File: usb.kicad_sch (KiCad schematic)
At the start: 55 parts, among them J901 AU-Y1008-2-BLK, J902 AU-Y1008-2-BLK, U901 USB2514B/M2, U902 AP22966DC8-7, U903 AP22966DC8-7, U904 USBLC6-2SC6, U905 USBLC6-2SC6, U906 USBLC6-2SC6, U907 USBLC6-2SC6, Y901 24 MHz

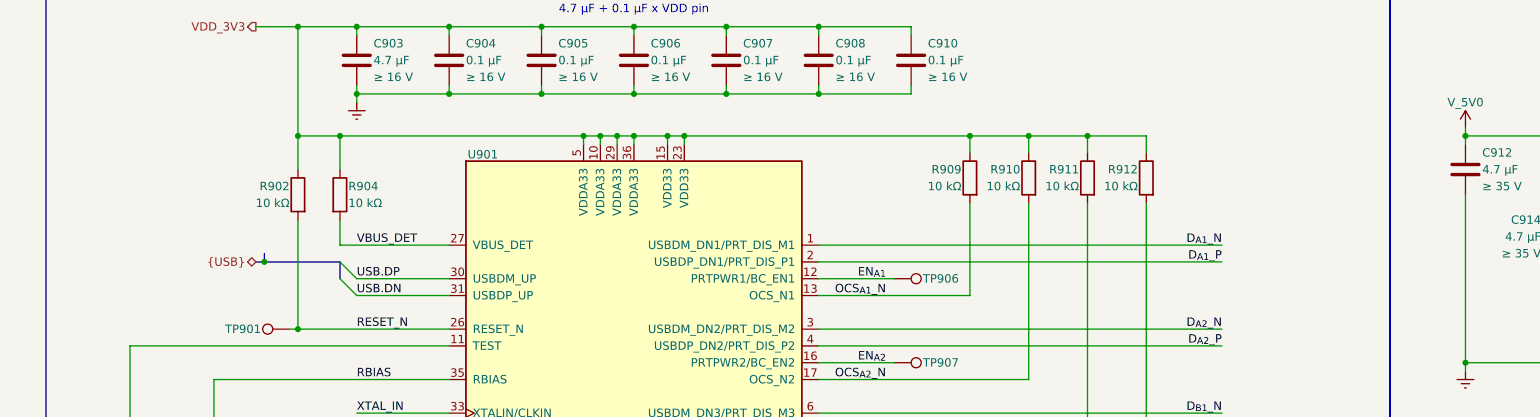
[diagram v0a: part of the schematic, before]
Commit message: Redo MPU pinout using STM32CubeMx
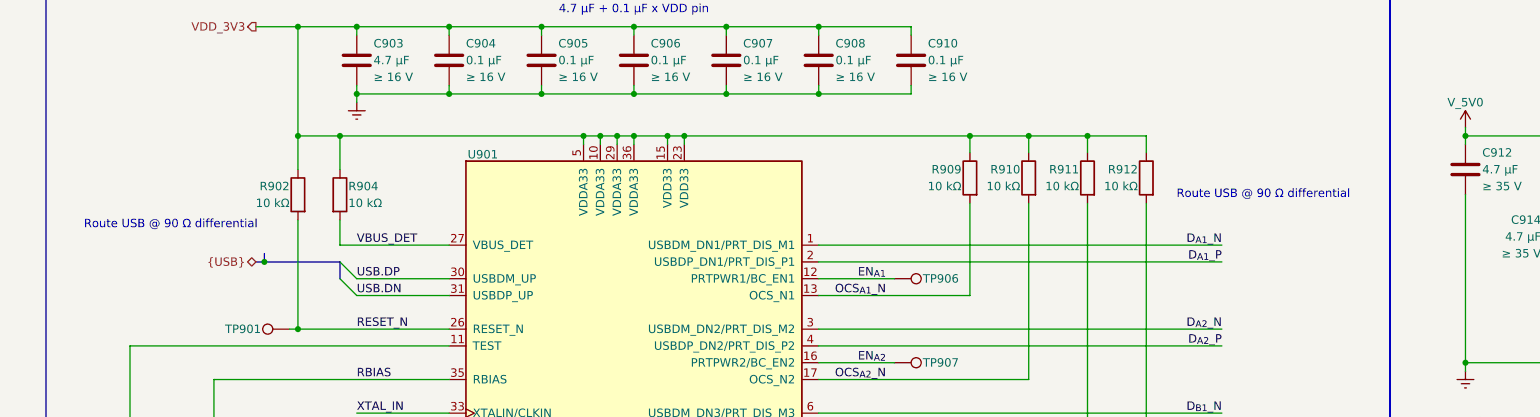
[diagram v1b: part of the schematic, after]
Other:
- note added: "Route USB @ 90 Ω differential"
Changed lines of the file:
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@@
 		)
 	)
+	(text "Route USB @ 90 Ω differential"
+		(exclude_from_sim no)
+		(at 183.642 114.3 0)
+		(effects
+			(font
+				(size 1.27 1.27)
+				(color 194 0 194 1)
+			)
+			(justify left)
+		)
+	)
 	(text "4.7 µF + 0.1 µF x VDD pin"
 		(exclude_from_sim no)
@@
 		)
 	)
+	(text "Route USB @ 90 Ω differential"
+		(exclude_from_sim no)
+		(at 44.704 118.872 0)
+		(effects
+			(font
+				(size 1.27 1.27)
+				(color 194 0 194 1)
+			)
+			(justify right)
+		)
+	)
 	(text "Ports A[0..1]"
 		(exclude_from_sim no)
@@
 		)
 		(property "Netclass" "USB"
-			(at 46.4185 120.65 0)
+			(at 45.0215 120.65 0)
 			(effects
 				(font
 					(size 1.27 1.27)
 				)
-				(justify left)
+				(justify right)
 			)
 		)
 		(property "Component Class" ""
-			(at 137.16 12.7 0)
+			(at -45.72 12.7 0)
 			(effects
 				(font
@@
 					(italic yes)
 				)
-				(justify left)
+				(justify right)
 			)
 		)

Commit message: Add additional info to passives
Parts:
- removed C920, C921, C922, C923: 220 µF, symbol Device:C
- added C920, C921, C922, C923: 220 µF, symbol Device:C_Polarized
- C901, C902, C904, C905, C906, C907, C908, C910: Size (none) -> 0402; Temperature coefficient (none) -> X5R; Tolerance (none) -> 20 %; Voltage rating ≥ 16 V -> 16 V
- C903: Size (none) -> 0603; Temperature coefficient (none) -> X5R; Tolerance (none) -> 20 %; Voltage rating ≥ 16 V -> 35 V
- C909, C911: Size (none) -> 0402; Tolerance (none) -> 2 %; Voltage rating (none) -> 35 V
- C912, C913, C914, C915: Size (none) -> 0603; Temperature coefficient (none) -> X5R; Tolerance (none) -> 20 %; Voltage rating ≥ 35 V -> 35 V
- C916, C917, C918, C919: Size (none) -> 0402; Temperature coefficient (none) -> X5R; Tolerance (none) -> 20 %; Voltage rating ≥ 35 V -> 35 V
- R901: Power rating (none) -> 0.1 W; Size (none) -> 0402; Tolerance ± 1 % -> 1 %
- R902, R904, R908, R909, R910, R911, R912: MPN 560112110020 -> (none); Manufacturer Würth Elektronik -> (none); Power rating (none) -> 0.1 W; Size (none) -> 0402; Tolerance (none) -> 1 %
- R903, R905, R906, R907: MPN 560112110019 -> (none); Manufacturer Würth Elektronik -> (none); Power rating (none) -> 0.1 W; Size (none) -> 0402; Tolerance (none) -> 1 %
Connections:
- net GND: now also C920.2, C921.2, C922.2, C923.2
- net NON_REM0: now also R908.1; no longer R908.2
- net V_BUS_{A1}: now also C920.1
- net V_BUS_{A2}: now also C922.1
- net V_BUS_{B1}: now also C921.1
- net V_BUS_{B2}: now also C923.1
- net at D901.2 (A): now also R908.2; no longer R908.1

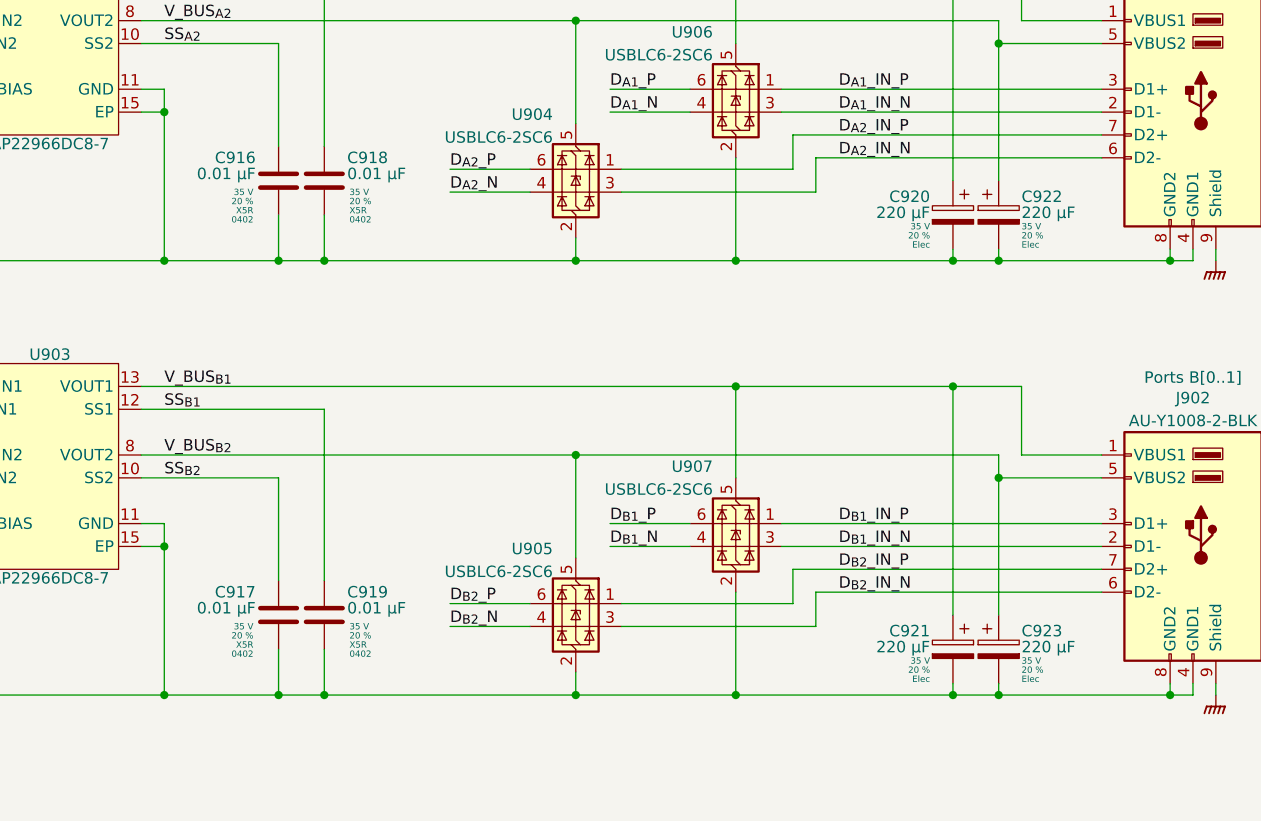
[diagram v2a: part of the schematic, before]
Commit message: Update capacitor BOM
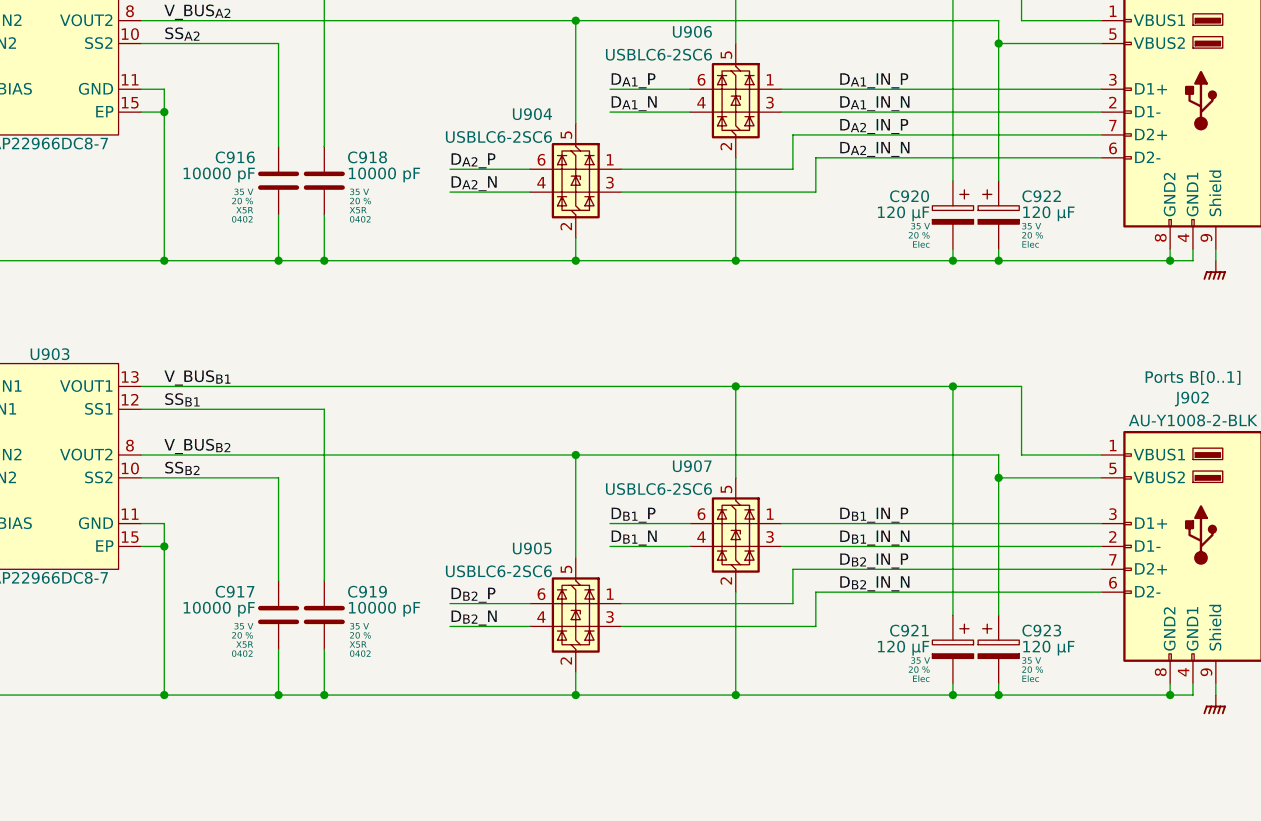
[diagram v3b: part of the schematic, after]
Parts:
- C901, C902, C904, C905, C906, C907, C908, C910: footprint (none) -> perfect_footprints:C_0402_1005Metric; Digi-Key Part Number (none) -> 490-10700-1-ND; MPN (none) -> GRM155R71H104KE14D; Manufacturer (none) -> Murata Electronics
- C903, C912, C913, C914, C915: footprint (none) -> Capacitor_SMD:C_0603_1608Metric; Digi-Key Part Number (none) -> 490-7205-1-ND; MPN (none) -> GRM188R6YA475KE15D; Manufacturer (none) -> Murata Electronics
- C909, C911: footprint (none) -> perfect_footprints:C_0402_1005Metric; Digi-Key Part Number (none) -> 490-3109-1-ND; MPN (none) -> GJM1555C1H8R0CB01D; Manufacturer (none) -> Murata Electronics
- C916, C917, C918, C919: value 0.01 µF -> 10000 pF; footprint (none) -> perfect_footprints:C_0402_1005Metric; Digi-Key Part Number (none) -> 490-4516-1-ND; MPN (none) -> GRM155R71H103KA88D; Manufacturer (none) -> Murata Electronics
- C920, C921, C922, C923: value 220 µF -> 120 µF; footprint (none) -> Capacitor_THT:C_Radial_D8.0mm_H11.5mm_P3.50mm; Digi-Key Part Number (none) -> 732-8943-1-ND; MPN (none) -> 860020574009; Manufacturer (none) -> Würth Elektronik

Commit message: Update R & L BOM
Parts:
- R901: Digi-Key Part Number (none) -> P12.1KLCT-ND; MPN (none) -> ERJ-2RKF1212X; Manufacturer (none) -> Panasonic Electronic Components
- R902, R904, R909, R910, R911, R912: Digi-Key Part Number (none) -> P10.0KLCT-ND; MPN (none) -> ERJ-2RKF1002X; Manufacturer (none) -> Panasonic Electronic Components
- R903, R905, R906, R907: Digi-Key Part Number (none) -> P100KLCT-ND; MPN (none) -> ERJ-2RKF1003X; Manufacturer (none) -> Panasonic Electronic Components
- R908: Digi-Key Part Number (none) -> P1.00KLCT-ND; MPN (none) -> ERJ-2RKF1001X; Manufacturer (none) -> Panasonic Electronic Components

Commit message: Fill BOM info
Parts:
- D901: Digi-Key Part Number (none) -> 732-4978-1-ND
- Y901: footprint (none) -> Crystal:Crystal_SMD_3225-4Pin_3.2x2.5mm; Digi-Key Part Number (none) -> 50-ECS-160-9-33B-CKM-TR3CT-ND; MPN (none) -> ECS-160-9-33B-CKM-TR3; Manufacturer (none) -> ECS Inc.
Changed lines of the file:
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@@
 			)
 		)
+		(property "Digi-Key Part Number" "732-4978-1-ND"
+			(at 153.67 208.28 90)
+			(effects
+				(font
+					(size 1.27 1.27)
+				)
+				(hide yes)
+			)
+		)
 		(pin "2"
 		)
@@
 			)
 		)
-		(property "Footprint" ""
+		(property "Footprint" "Crystal:Crystal_SMD_3225-4Pin_3.2x2.5mm"
 			(at 148.59 176.53 0)
 			(effects
@@
 			)
 		)
-		(property "Datasheet" "~"
+		(property "Datasheet" "https://ecsxtal.com/store/pdf/ECS-33B.pdf"
+			(at 148.59 176.53 0)
+			(effects
+				(font
+					(size 1.27 1.27)
+				)
+				(hide yes)
+			)
+		)
+		(property "Description" "16 MHz ±10ppm Crystal 9pF 60 Ohms 4-SMD, No Lead"
+			(at 148.59 176.53 0)
+			(effects
+				(font
+					(size 1.27 1.27)
+				)
+				(hide yes)
+			)
+		)
+		(property "Digi-Key Part Number" "50-ECS-160-9-33B-CKM-TR3CT-ND"
+			(at 148.59 176.53 0)
+			(effects
+				(font
+					(size 1.27 1.27)
+				)
+				(hide yes)
+			)
+		)
+		(property "MPN" "ECS-160-9-33B-CKM-TR3"
 			(at 148.59 176.53 0)
 			(effects
@@
 			)
 		)
-		(property "Description" "Four pin crystal, GND on pins 2 and 4"
+		(property "Manufacturer" "ECS Inc."
 			(at 148.59 176.53 0)
 			(effects

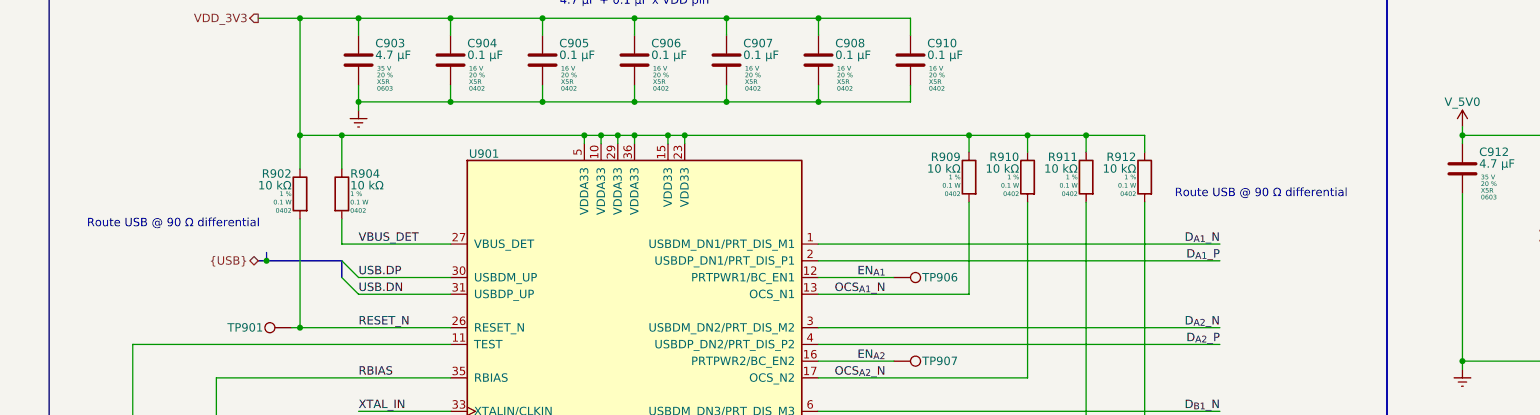
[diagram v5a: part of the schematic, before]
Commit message: Fill BOM information for the rest
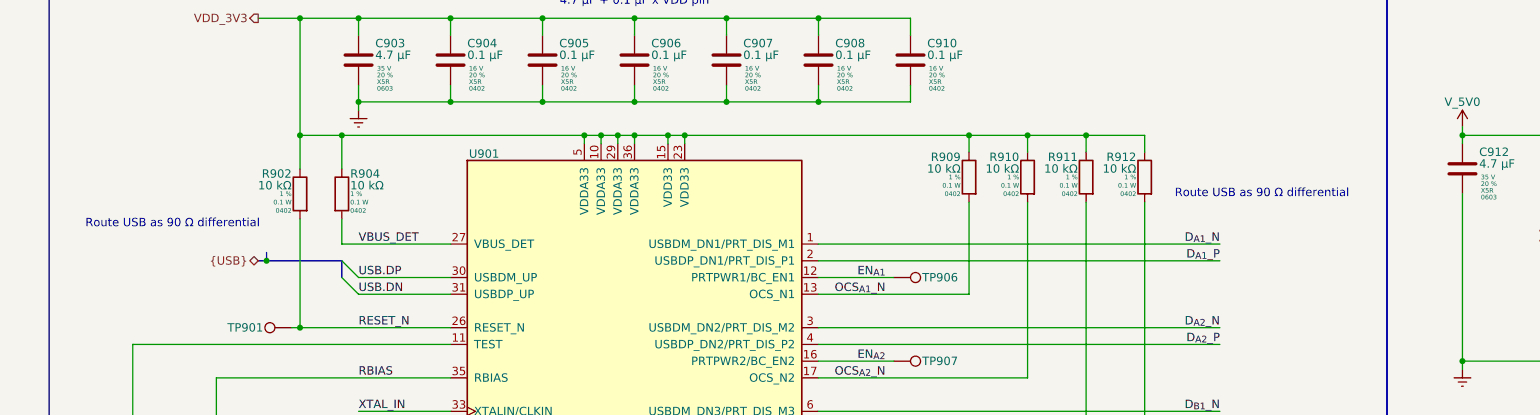
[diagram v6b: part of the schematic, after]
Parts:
- U904, U905, U906, U907: Digi-Key Part Number (none) -> 497-5235-1-ND; MPN (none) -> USBLC6-2SC6; Manufacturer (none) -> STMicroelectronics
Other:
- note added: "Route USB as 90 Ω differential"
- note removed: "Route USB @ 90 Ω differential"
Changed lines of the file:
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@@
 		)
 	)
-	(text "Route USB @ 90 Ω differential"
+	(text "Route USB as 90 Ω differential"
 		(exclude_from_sim no)
 		(at 183.642 114.3 0)
@@
 		)
 	)
-	(text "Route USB @ 90 Ω differential"
+	(text "Route USB as 90 Ω differential"
 		(exclude_from_sim no)
 		(at 44.704 118.872 0)
@@
 			)
 		)
-		(property "Datasheet" "~"
+		(property "Datasheet" "https://www.assmann-wsw.com/uploads/datasheets/ASS_5781_CO.pdf"
 			(at 388.62 170.18 0)
 			(effects
@@
 			)
 		)
-		(property "Description" "USB Type A connector, stacked"
+		(property "Description" "USB-A (USB TYPE-A) USB 2.0 Receptacle Connector 8 Position Through Hole, Right Angle"
 			(at 393.7 171.45 0)
 			(effects
@@
 			)
 		)
-		(property "Datasheet" "https://www.st.com/resource/en/datasheet/usblc6-2.pdf"
+		(property "Datasheet" "https://www.st.com/resource/en/datasheet/cd00050750.pdf"
 			(at 341.63 177.165 0)
 			(effects
@@
 			)
 		)
-		(property "Description" "Very low capacitance ESD protection diode, 2 data-line, SOT-23-6"
+		(property "Description" "17V Clamp 5A (8/20µs) Ipp Tvs Diode Surface Mount SOT-23-6"
+			(at 342.9 168.91 0)
+			(effects
+				(font
+					(size 1.27 1.27)
+				)
+				(hide yes)
+			)
+		)
+		(property "Digi-Key Part Number" "497-5235-1-ND"
+			(at 342.9 168.91 0)
+			(effects
+				(font
+					(size 1.27 1.27)
+				)
+				(hide yes)
+			)
+		)
+		(property "MPN" "USBLC6-2SC6"
+			(at 342.9 168.91 0)
+			(effects
+				(font
+					(size 1.27 1.27)
+				)
+				(hide yes)
+			)
+		)
+		(property "Manufacturer" "STMicroelectronics"
 			(at 342.9 168.91 0)
 			(effects
@@
 			)
 		)
-		(property "Datasheet" "https://www.st.com/resource/en/datasheet/usblc6-2.pdf"
+		(property "Datasheet" "https://www.st.com/resource/en/datasheet/cd00050750.pdf"
 			(at 323.85 137.795 0)
 			(effects
@@
 			)
 		)
-		(property "Description" "Very low capacitance ESD protection diode, 2 data-line, SOT-23-6"
+		(property "Description" "17V Clamp 5A (8/20µs) Ipp Tvs Diode Surface Mount SOT-23-6"
+			(at 325.12 129.54 0)
+			(effects
+				(font
+					(size 1.27 1.27)
+				)
+				(hide yes)
+			)
+		)
+		(property "Digi-Key Part Number" "497-5235-1-ND"
+			(at 325.12 129.54 0)
+			(effects
+				(font
+					(size 1.27 1.27)
+				)
+				(hide yes)
+			)
+		)
+		(property "MPN" "USBLC6-2SC6"
+			(at 325.12 129.54 0)
+			(effects
+				(font
+					(size 1.27 1.27)
+				)
+				(hide yes)
+			)
+		)
+		(property "Manufacturer" "STMicroelectronics"
 			(at 325.12 129.54 0)
 			(effects
@@
 			)
 		)
-		(property "Datasheet" "~"
+		(property "Datasheet" "https://www.assmann-wsw.com/uploads/datasheets/ASS_5781_CO.pdf"
 			(at 388.62 121.92 0)
 			(effects
@@
 			)
 		)
-		(property "Description" "USB Type A connector, stacked"
+		(property "Description" "USB-A (USB TYPE-A) USB 2.0 Receptacle Connector 8 Position Through Hole, Right Angle"
 			(at 393.7 123.19 0)
 			(effects
@@
 			)
 		)
-		(property "Datasheet" "https://www.st.com/resource/en/datasheet/usblc6-2.pdf"
+		(property "Datasheet" "https://www.st.com/resource/en/datasheet/cd00050750.pdf"
 			(at 323.85 186.055 0)
 			(effects
@@
 			)
 		)
-		(property "Description" "Very low capacitance ESD protection diode, 2 data-line, SOT-23-6"
+		(property "Description" "17V Clamp 5A (8/20µs) Ipp Tvs Diode Surface Mount SOT-23-6"
+			(at 325.12 177.8 0)
+			(effects
+				(font
+					(size 1.27 1.27)
+				)
+				(hide yes)
+			)
+		)
+		(property "Digi-Key Part Number" "497-5235-1-ND"
+			(at 325.12 177.8 0)
+			(effects
+				(font
+					(size 1.27 1.27)
+				)
+				(hide yes)
+			)
+		)
+		(property "MPN" "USBLC6-2SC6"
+			(at 325.12 177.8 0)
+			(effects
+				(font
+					(size 1.27 1.27)
+				)
+				(hide yes)
+			)
+		)
+		(property "Manufacturer" "STMicroelectronics"
 			(at 325.12 177.8 0)
 			(effects
@@
 			)
 		)
-		(property "Datasheet" "https://www.st.com/resource/en/datasheet/usblc6-2.pdf"
+		(property "Datasheet" "https://www.st.com/resource/en/datasheet/cd00050750.pdf"
 			(at 341.63 128.905 0)
 			(effects
@@
 			)
 		)
-		(property "Description" "Very low capacitance ESD protection diode, 2 data-line, SOT-23-6"
+		(property "Description" "17V Clamp 5A (8/20µs) Ipp Tvs Diode Surface Mount SOT-23-6"
+			(at 342.9 120.65 0)
+			(effects
+				(font
+					(size 1.27 1.27)
+				)
+				(hide yes)
+			)
+		)
+		(property "Digi-Key Part Number" "497-5235-1-ND"
+			(at 342.9 120.65 0)
+			(effects
+				(font
+					(size 1.27 1.27)
+				)
+				(hide yes)
+			)
+		)
+		(property "MPN" "USBLC6-2SC6"
+			(at 342.9 120.65 0)
+			(effects
+				(font
+					(size 1.27 1.27)
+				)
+				(hide yes)
+			)
+		)
+		(property "Manufacturer" "STMicroelectronics"
 			(at 342.9 120.65 0)
 			(effects
